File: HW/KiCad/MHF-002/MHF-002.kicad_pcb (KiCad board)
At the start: 4 copper layers, 100 x 100 mm, 305 parts, among them J1 VGA, J10 I2C, J100 x, J101 x, J102 x, J103 x, J104 x, J105 x, J106 x, J107 +3V3, J108 GND, J109 +3V3, J11 + 5V -, J110 +5V, J111 GND, J112 GND, J113 SDCard, J114 VIN, J115 VI, J116 GND, J12 Reset, J13 +5V, J14 GND, J15 AREF, J16 XTAL2, J17 SDcard, J18 XTAL1, J19 AVCC, J2 PS/2, J21 x, J22 x, J23 VIN 12V, J24 AND_B1, J25 AND_B2, J26 AND_C1, J27 AND_C2, J28 AND_D1, J29 AND_D2, J3 RCA, J30 AND_Dx, J31 AND_Cx, J32 AND_Bx, J33 NOTF, J34 NOTE, J35 NOTEx, J36 NOTFx, J37 x, J38 x, J39 x, J4 SysBus, J40 x, J41 x, J42 x, J43 x, J44 x, J45 x, J46 x, J47 x, J48 x, J49 x, J5 Micro, J50 x, J51 x, J52 x, J53 x, J54 x, J55 x, J56 x, J57 x, J58 x, J59 x, J6 SysBus, J60 x, J61 x, J62 x, J63 x, J64 x, J65 x, J66 x, J67 x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

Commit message: D-Latch testpoints
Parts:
- added TP1: 7, MHF:TestPoint_Pad_1.0x1.0mm, F.Cu at (199.9, 66.1)
- added TP2: 0, MHF:TestPoint_Pad_1.0x1.0mm, F.Cu at (169.3, 67.6)
- added TP3: 1, MHF:TestPoint_Pad_1.0x1.0mm, F.Cu at (171.1, 67.6)
- added TP4: 2, MHF:TestPoint_Pad_1.0x1.0mm, F.Cu at (169.3, 65.8)
- added TP5: 3, MHF:TestPoint_Pad_1.0x1.0mm, F.Cu at (171.1, 65.8)
- added TP6: 4, MHF:TestPoint_Pad_1.0x1.0mm, F.Cu at (198.3, 67.7)
- added TP7: 5, MHF:TestPoint_Pad_1.0x1.0mm, F.Cu at (199.9, 67.7)
- added TP8: 6, MHF:TestPoint_Pad_1.0x1.0mm, F.Cu at (198.3, 66.1)
- C1: value 10 nF -> 10nF
- moved JP102 10.2 mm to (167.0, 80.0), turned to 0 degrees
- moved JP104 10.2 mm to (177.2, 80.0), turned to 0 degrees
- moved JP100 5.08 mm to (172.1, 76.2), turned to 0 degrees
- moved JP99 5.08 mm to (167.0, 76.2), turned to 0 degrees
- moved Cx4 2.57 mm to (202.9, 104.2), turned to 90 degrees
- turned JP103 to 0 degrees
- turned JP105 to 0 degrees
- turned JP106 to 0 degrees
- turned JP107 to 0 degrees
- turned JP92 to 0 degrees
- turned JP98 to 0 degrees
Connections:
- J1 pad 0: unconnected-(J1-Pad0) -> GND
- J4 pad 45: A_G_D_DIR -> A_G_ENABLE
- J4 pad 46: B_G_D_DIR -> B_G_ENABLE
- J4 pad 49: A_G_ENABLE -> A_G_D_DIR
- J4 pad 50: B_G_ENABLE -> B_G_D_DIR
- J6 pad 45: A_G_D_DIR -> A_G_ENABLE
- J6 pad 46: B_G_D_DIR -> B_G_ENABLE
- J6 pad 49: A_G_ENABLE -> A_G_D_DIR
- J6 pad 50: B_G_ENABLE -> B_G_D_DIR
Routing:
- net A_S_ENABLE: track 30.6 -> 14.3 mm
- net B_S_ENABLE: track 26.8 -> 14.5 mm
- net B_S_WRITE: track 17.0 -> 28.4 mm, vias 1 -> 0
- net A_G_ENABLE: track 28.4 -> 17.6 mm
- net Shared_Address_A14: track 99.3 -> 89.7 mm, vias 4 -> 3
- net A_SHARE_GRANTED: track 22.3 -> 13.0 mm
- net S_ENABLE: track 80.2 -> 72.7 mm
- net Bb: track 133.7 -> 126.7 mm
- net B_SHARE_REQUEST: track 13.9 -> 19.9 mm, vias 1 -> 0
- net A_S_READ: track 26.5 -> 20.5 mm
- net /L5: track 14.3 -> 19.4 mm
- net /L2: track 15.3 -> 20.4 mm
- net B16: track 20.9 -> 25.9 mm
- net /L0: track 14.2 -> 19.1 mm
- net B_G_ENABLE: track 21.1 -> 16.5 mm
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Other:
- board text added: "16"
- board text added: "5V"
- board text added: "Adir"
- board text added: "AxB"
- board text added: "DTR"
- board text added: "Ddir"
- board text added: "Dirty"
- board text added: "Ext RAM"
- board text added: "G_En"
- board text added: "Grant"
- board text added: "HALT"
- board text added: "Read"
- board text added: "Req"
- board text added: "S_En"
- board text added: "S_Rd"
- board text added: "S_Wr"
- board text removed: "SDcard"

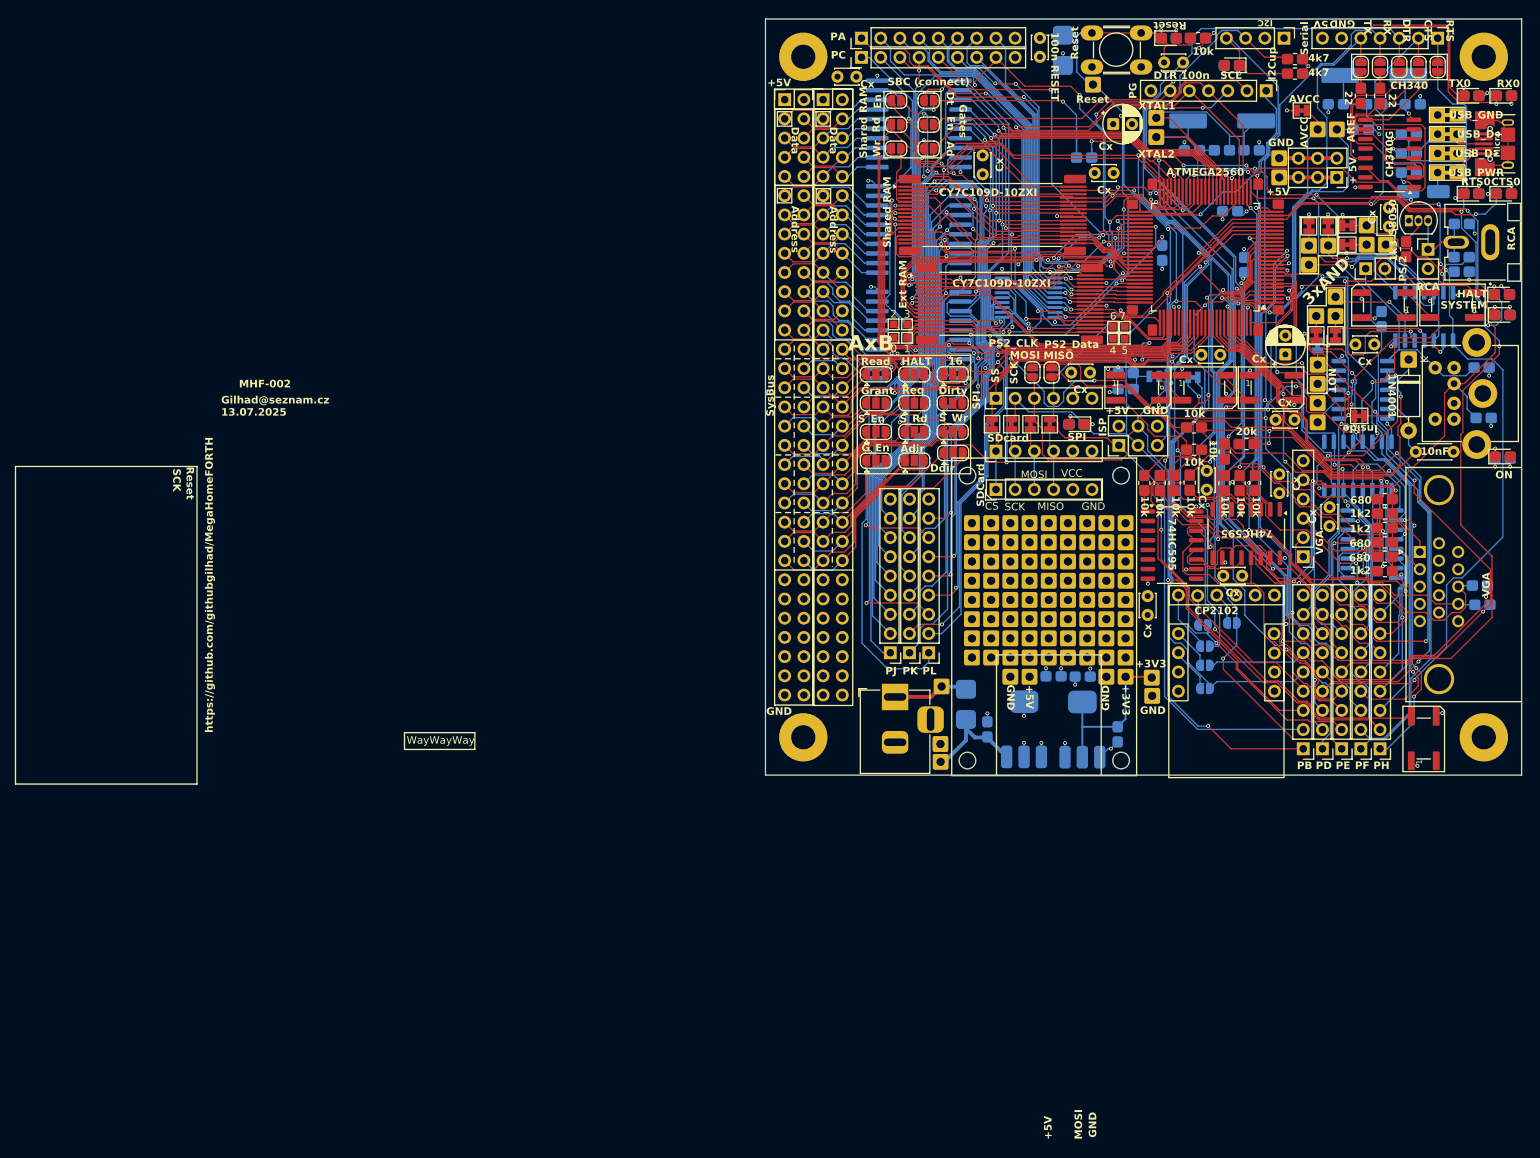
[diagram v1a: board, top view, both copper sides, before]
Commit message: reset + I2C LED
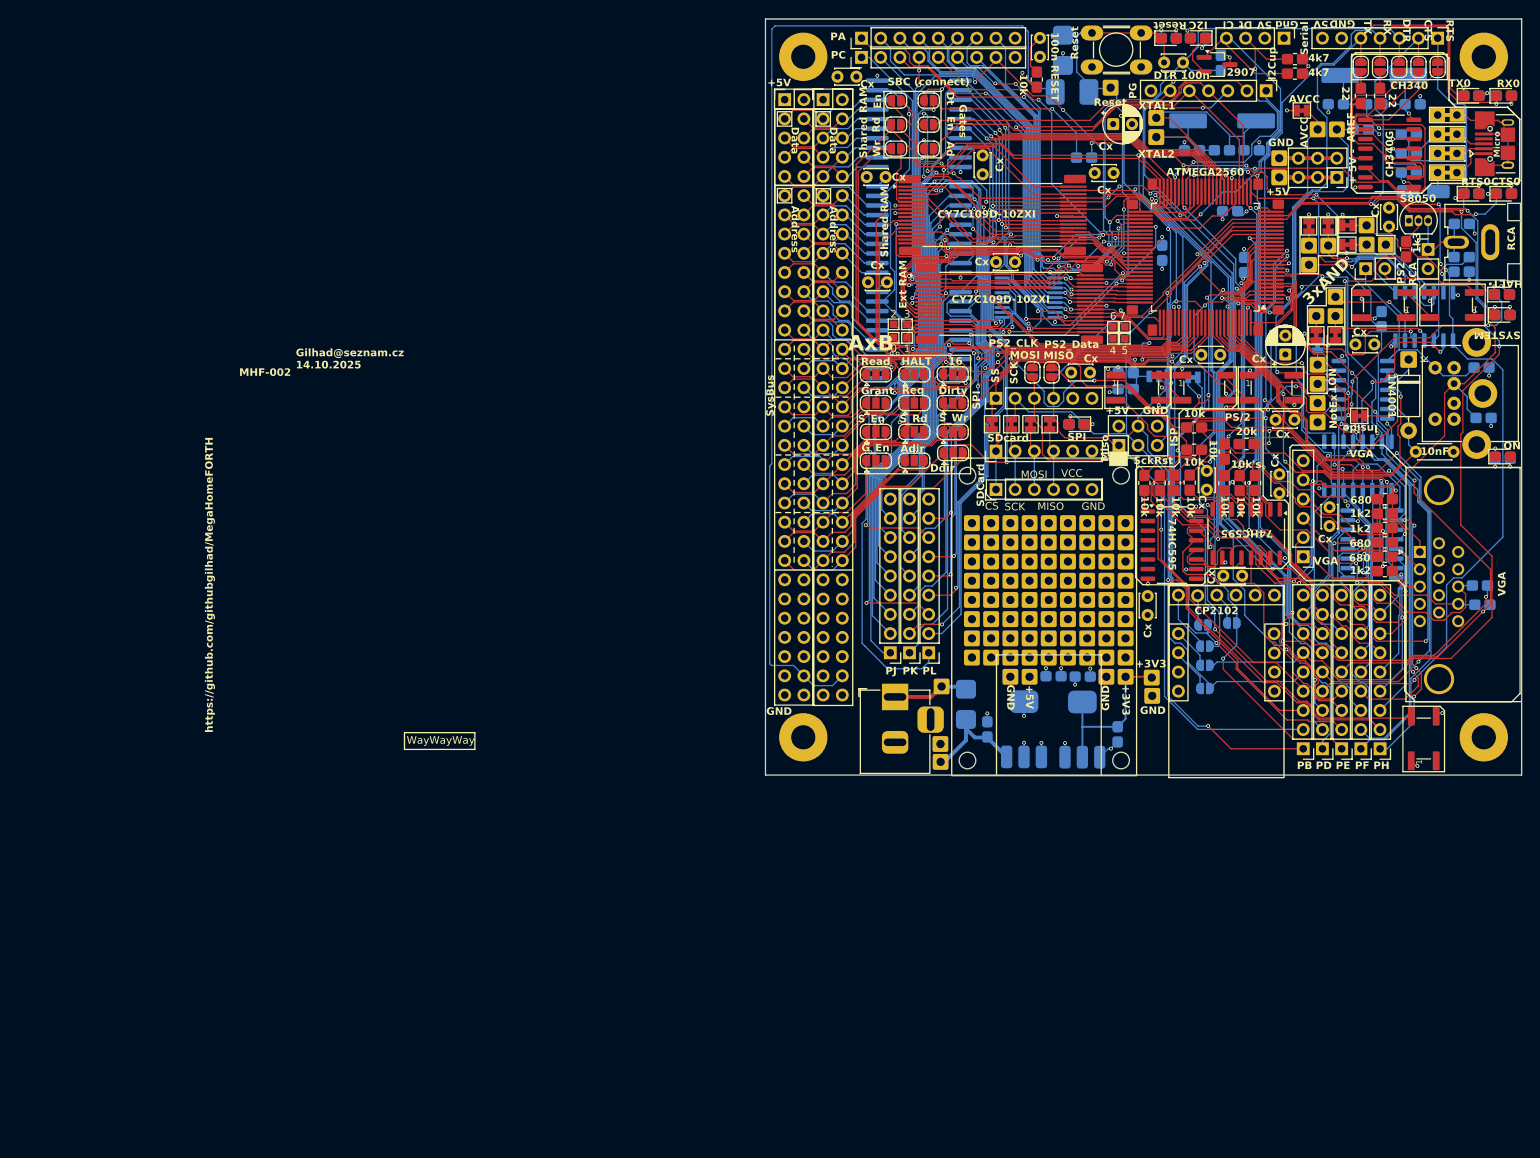
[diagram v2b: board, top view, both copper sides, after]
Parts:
- added Cx16: Cx, MHF:C_Disc_D3.0mm_W2.0mm_P2.50mm, F.Cu at (168.5, 60.2)
- added Cx17: Cx, MHF:C_Disc_D3.0mm_W2.0mm_P2.50mm, F.Cu at (168.3, 46.3)
- added Cx18: Cx, MHF:C_Disc_D3.0mm_W2.0mm_P2.50mm, F.Cu at (182.9, 57.6)
- added D10: SS14, MHF:D_1812_4532Metric_Pad1.30x3.40mm_HandSolder, B.Cu at (192.9, 35.1)
- added Q2: 2907, MHF:TSOT-23_HandSoldering, F.Cu at (212.1, 31.4)
- JP26: value PS/2 -> PS2
- R40: value HALTdown 1k -> 1k
- R42: value HALTup 1k -> 1k
- moved R26 22.0 mm to (188.3, 33.4), turned to 90 degrees
- moved LED6 5.76 mm to (209.6, 27.9)
- moved R39 5.76 mm to (209.6, 27.9)
- moved R28 4.47 mm to (212.6, 31.2), turned to -90 degrees
- moved J12 2.37 mm to (198.0, 34.5)
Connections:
- J4 pad 62: unconnected-(J4-Pin_62-Pad62) -> MasterReset
- J6 pad 62: unconnected-(J6-Pin_62-Pad62) -> MasterReset
- LED6 pad 1: SCL -> Net-(LED6-K)
- M3 pad 13: /L4 -> /L3
- M3 pad 14: /L5 -> /L2
- M3 pad 15: /L6 -> /L1
- M3 pad 16: /L7 -> /L0
- M3 pad 17: /L3 -> /L4
- M3 pad 18: /L2 -> /L5
- M3 pad 19: /L1 -> /L6
- M3 pad 20: /L0 -> /L7
- TP1 pad 1: /L0 -> /L7
- TP2 pad 1: /L7 -> /L0
- TP3 pad 1: /L6 -> /L1
- TP4 pad 1: /L5 -> /L2
- TP5 pad 1: /L4 -> /L3
- TP6 pad 1: /L3 -> /L4
- TP7 pad 1: /L2 -> /L5
- TP8 pad 1: /L1 -> /L6
- U4 pad 12: /L7 -> /L0
- U4 pad 13: /L6 -> /L1
- U4 pad 14: /L5 -> /L2
- U4 pad 15: /L4 -> /L3
- U4 pad 16: /L3 -> /L4
- U4 pad 17: /L2 -> /L5
- U4 pad 18: /L1 -> /L6
- U4 pad 19: /L0 -> /L7
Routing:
- net MasterReset: track 0.00 -> 138.9 mm
- net SDA: track 125.4 -> 118.2 mm, vias 1 -> 3
- net Net-(LED6-K): track 0.00 -> 5.80 mm
- net X_SHARE_GRANTED: track 74.6 -> 69.2 mm
- net DTR: track 122.0 -> 127.0 mm
- net X_S16: track 155.3 -> 150.5 mm, vias 7 -> 5
- net SCL: track 126.5 -> 130.0 mm
- net X_HALT: track 72.4 -> 75.6 mm
- net Reset: track 96.1 -> 99.1 mm
- net XAA7: track 82.3 -> 79.3 mm
- net X_READ: track 147.7 -> 150.2 mm
- net RD: track 53.7 -> 52.1 mm
- net +5V: track 101.6 -> 103.0 mm, vias 55 -> 52
- net /L4: track 17.1 -> 18.3 mm
- net /L3: track 18.3 -> 17.1 mm
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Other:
- board text added: "10k's"
- board text added: "CInside"
- board text added: "Cl"
- board text added: "Gilhad@seznam.cz 14.10.2025"
- board text added: "Gnd"
- board text added: "Miso"
- board text added: "NotEx"
- board text added: "PS/2"
- board text added: "RCA"
- board text added: "Rst"
- board text added: "Sck"
- board text added: "VGA"
- board text added: "down"
- board text added: "up"
- board text removed: "AND"
- board text removed: "Gilhad@seznam.cz 13.07.2025"
- board text removed: "MOSI"
- board text removed: "Reset"
- board text removed: "SCK"
- board text removed: "up-HALT-dn"

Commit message: Final version of HW MHF-002
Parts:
- JP14: value AVCC -> xAVCC
- JP21: value TX2102 -> RX0
- JP22: value RX2102 -> TX0
- JP23: value CTS2102 -> RTS0
- JP24: value DTR2102 -> DTR0
- JP25: value RTS2102 -> CTS0
- moved JP14 2.00 mm to (225.3, 37.3), turned to -90 degrees
- moved JP23 0.36 mm to (210.3, 111.1)
- moved JP24 0.25 mm to (210.3, 108.4)
- moved JP25 0.25 mm to (210.3, 113.9)
- moved JP21 0.23 mm to (214.1, 105.5)
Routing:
- net GND: track 89.2 -> 98.5 mm
- net +5V: track 103.0 -> 104.9 mm
- net Net-(J19-Pin_1): track 35.2 -> 34.3 mm
- net TX0: track 152.4 -> 153.4 mm
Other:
- board text added: "3V3"
- board text added: "7-12V"
- board text added: "Gilhad@seznam.cz 17.10.2025"
- board text added: "USB"
- board text added: "[+center]"
- board text removed: "Gilhad@seznam.cz 14.10.2025"
